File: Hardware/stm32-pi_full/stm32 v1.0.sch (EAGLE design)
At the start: 292 parts, among them J1 SOLDERJUMPERNO, J2 5-1814400-1, U1 ESP32-WROOM-32D, X1 OPAMP, Y1 6MM_3.5MM_CRYSTAL

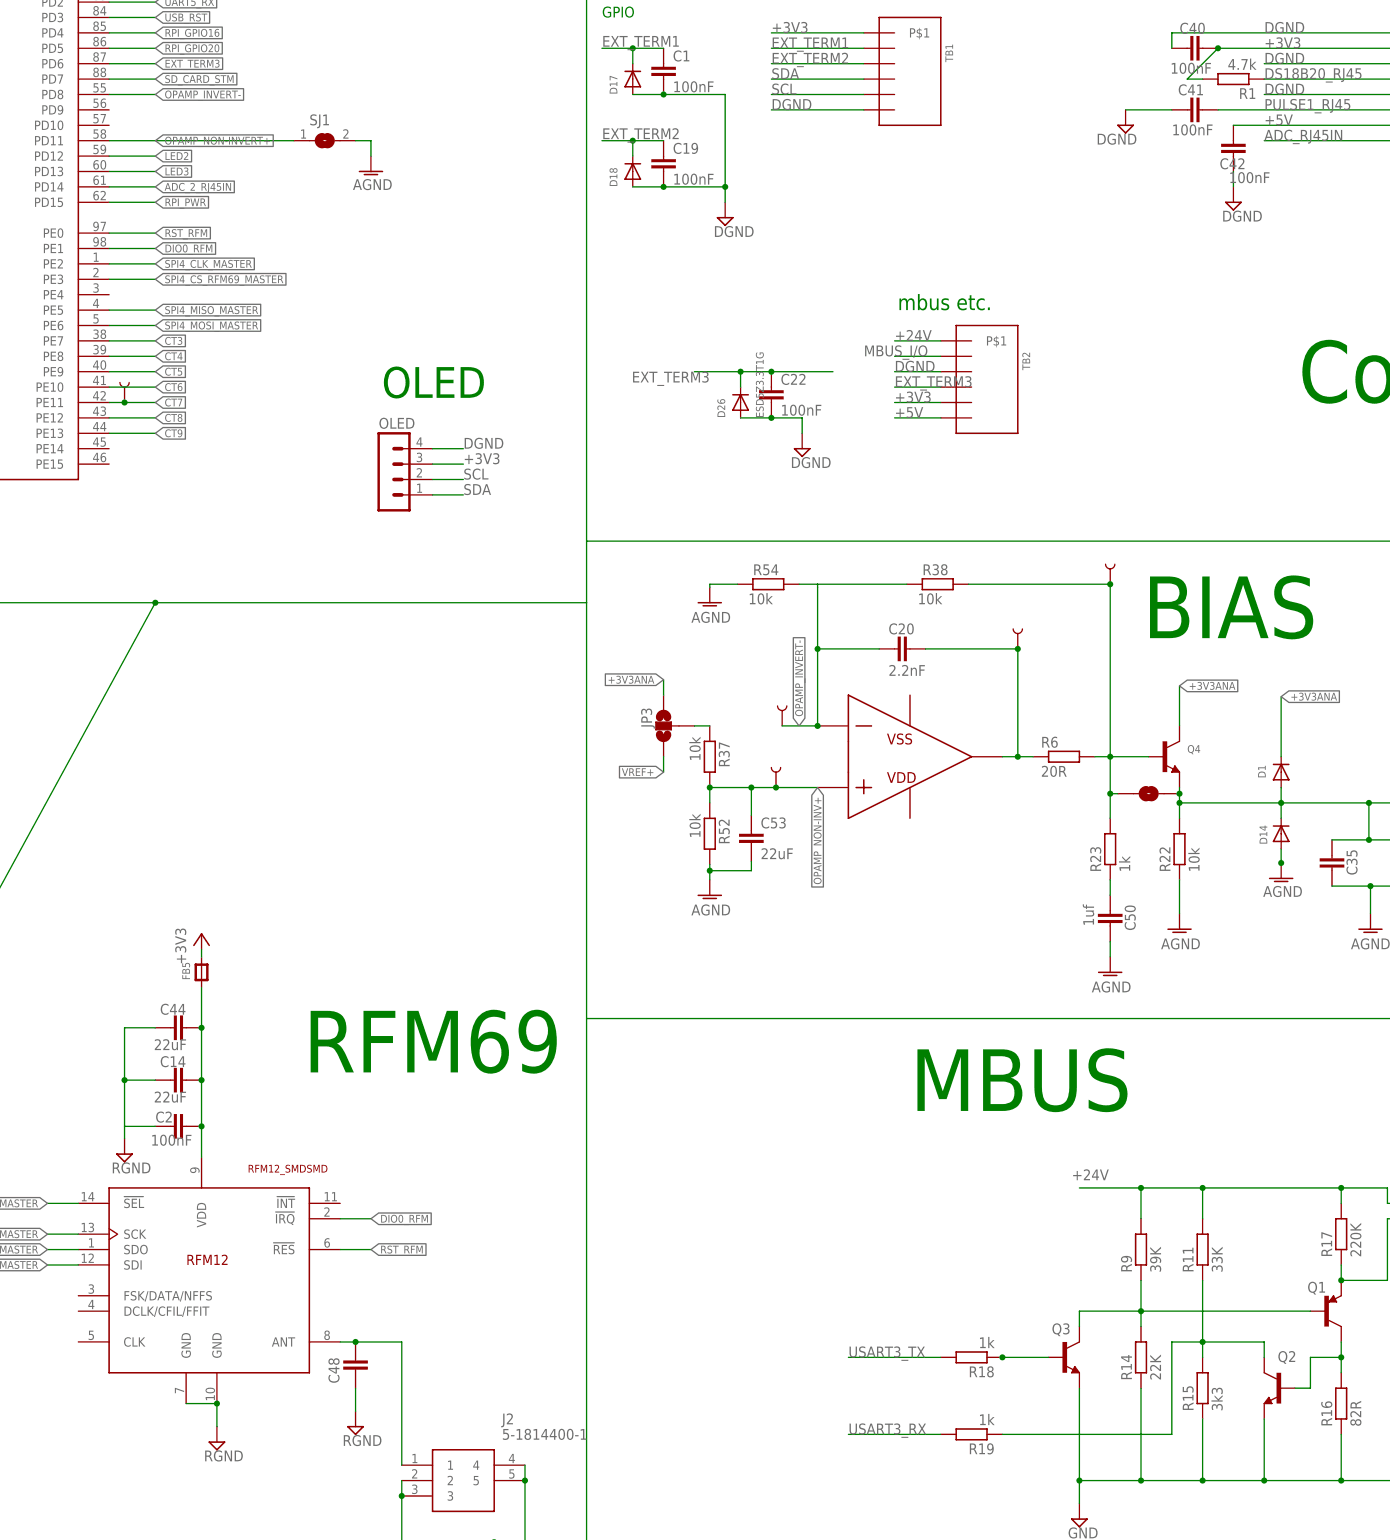
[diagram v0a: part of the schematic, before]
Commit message: UART Tx improvments and v1.0 HW change
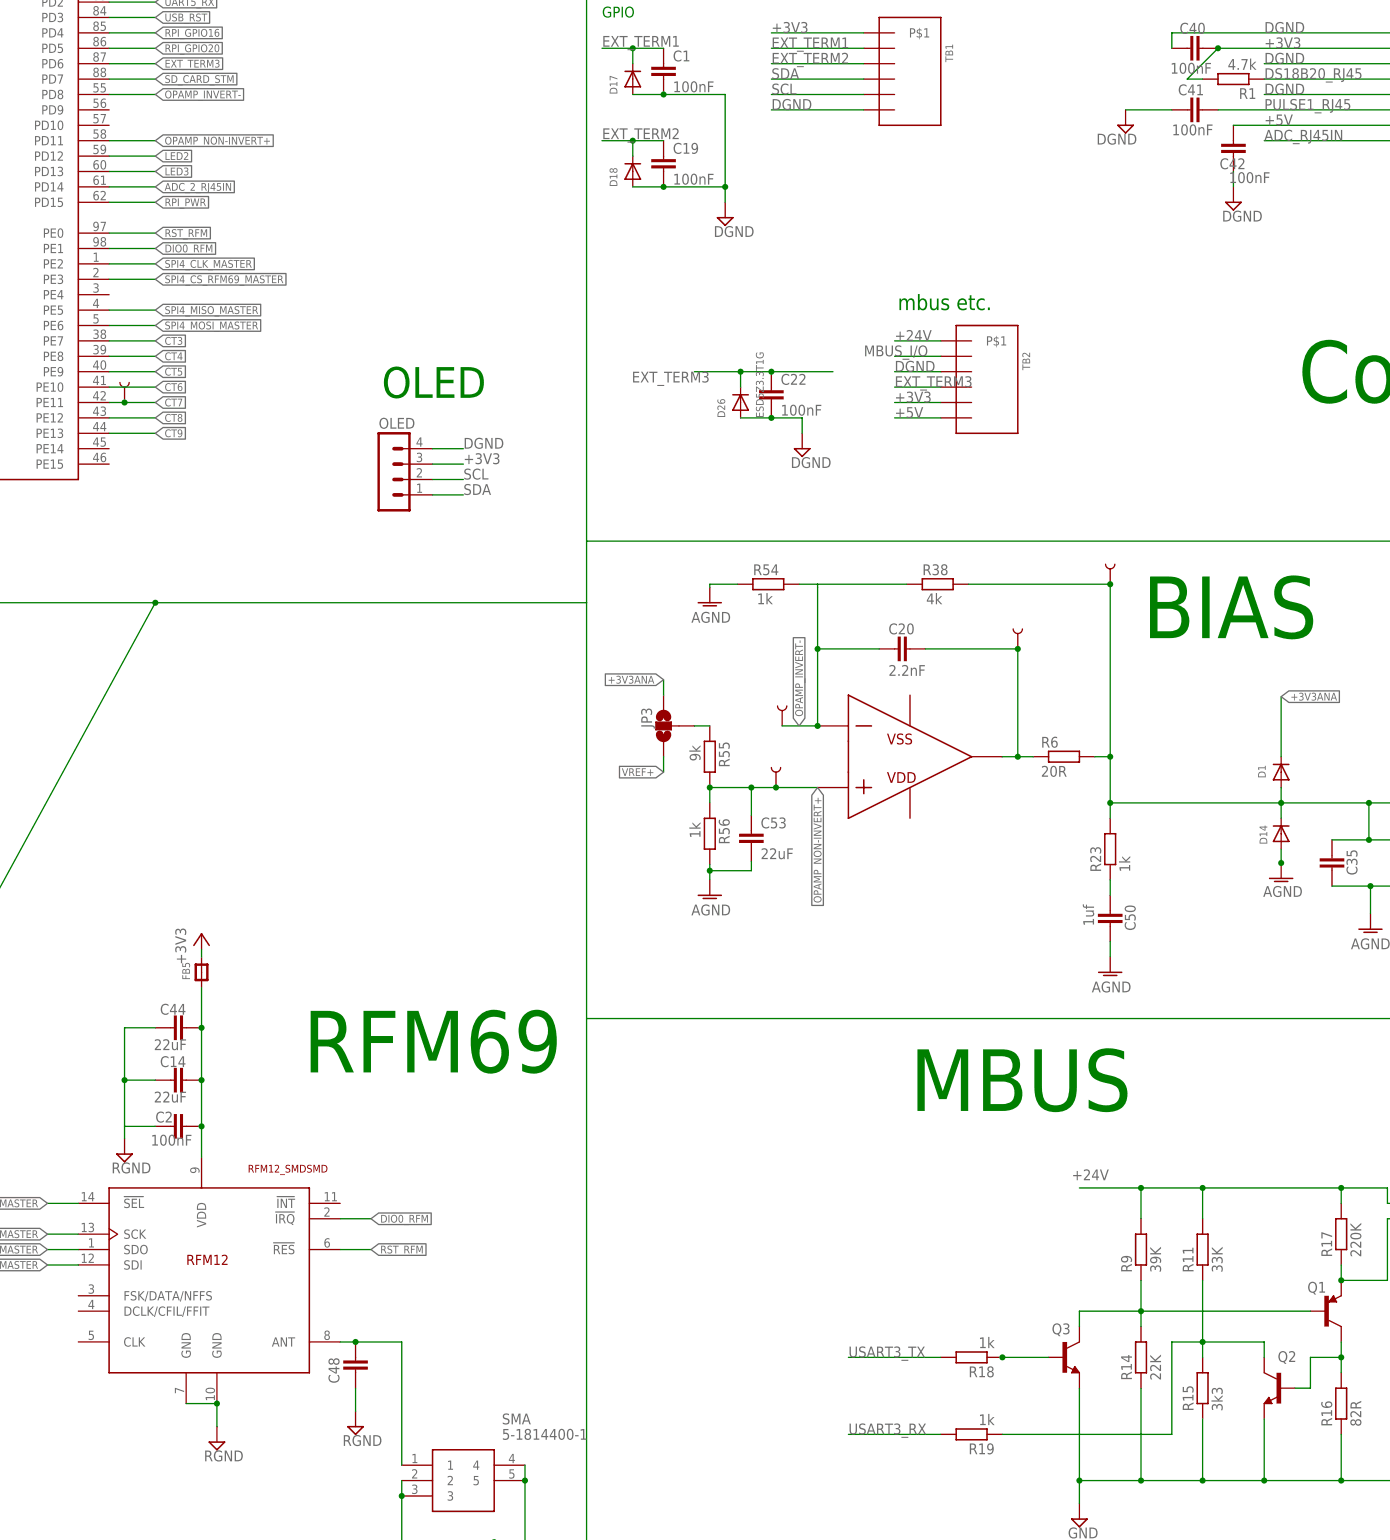
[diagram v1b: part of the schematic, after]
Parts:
- removed JP2: JUMPER-SMT_2_NO_NO-SILK, SparkFun-Jumpers:JUMPER-SMT_2_NO_NO-SILK
- removed Q4: (no value), microbuilder:TRANSISTOR_NPNWIDE
- removed R22: 10k, resistor:R-EU_R0603
- removed SJ1: (no value), jumper-con_db:SJ-CONCON
- R38: value 10k -> 4k
- R54, R56: value 10k -> 1k
- R55: value 10k -> 9k
- renumbered J2 to SMA, R37 to R55, R52 to R56
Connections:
- removed net OPAMP_FB2: JP2.1, Q4.B, R23.2, R38.1, R6.2, TP3.1
- removed net OPAMP_NON-INV+: C53.1, R55.1, R56.2, TP2.1, X1.P
- net +3V3ANA: no longer Q4.C
- net AGND: no longer R22.1, SJ1.2
- net BIAS: now also R23.2, R38.1, R6.2, TP3.1; no longer JP2.2, Q4.E, R22.2
- net OPAMP_NON-INVERT+: now also C53.1, R55.1, R56.2, TP2.1, X1.P; no longer SJ1.1

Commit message: commit v1.0 HW for prototype.
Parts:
- removed D14, D22, D23, D32, D36, D37: ESD5Z3.3T1G, microbuilder:DIODESOD-523
- removed EXPANSION: TSM-113-01-T-DV, pinhead+:PINHD-2X13SMT
- removed JP19, JP3: JUMPER-SMT_3_NO_NO-SILK, SparkFun-Jumpers:JUMPER-SMT_3_NO_NO-SILK
- removed R35, R36: 10k, rcl:R-EU_R0603
- removed SV1: (no value), con-lstb-db:MA06-1
- removed UART1: (no value), con-lstb-db:MA02-1
- removed X1: OPAMP, ngspice-simulation:OPAMP
- added D3: SCHOTTKY_MBR0520LT1GDO-219-AB(SOD123F), Diode:SCHOTTKY_MBR0520LT1GDO-219-AB(SOD123F)
- added D4: ESD5Z3.3T1G, microbuilder:DIODESOD-523
- added IC2: AD8519KS, analog-devices:AD8519KS
- added IC_VBAT: AP7313-33SRG-7, AP7313-33SRG-7:AP7313-33SRG-7
- added JP2: PINHD-2X7, Connector:PINHD-2X7
- added R22: 0R, rcl:R-EU_R0603
- added TP8: TEST-POINTPOGO_PTH, SparkFun-Connectors:TEST-POINTPOGO_PTH
- C23, C50: value 1uf -> 1uF
- C49: value 1nF -> 100nF
- C52: value 22UF -> 1uF; device rcl:C-EUC0805 -> resistor:C-EUC0603
- C7: value 22uF -> 1uF; device rcl:C-EUC0805 -> resistor:C-EUC0603
- D2: value ESD5Z3.3T1G -> SCHOTTKY_MBR0520LT1GDO-219-AB(SOD123F); device microbuilder:DIODESOD-523 -> Diode:SCHOTTKY_MBR0520LT1GDO-219-AB(SOD123F); MPN (none) -> MBR130LSFT1G
- J1, SJ14, SJ26, SJ27, SJ3, SJ32, SJ5, SJ6, SJ7: value SOLDERJUMPERNO -> JUMPER-SMT_2_NC_TRACE_NO-SILK; device SparkFun:SOLDERJUMPERNO -> SparkFun-Jumpers:JUMPER-SMT_2_NC_TRACE_NO-SILK
- Q1: value (none) -> PNP
- Q2, Q3: value (none) -> NPN
- R12, R24, R28: value 10K -> 10k
- R38: value 4k -> 39k
- R39, R40, R41: value 620 -> 620R
- R54, R56: value 1k -> 10k
- R55: value 9k -> 91k
- R6: value 20R -> 0R
- R8: value 100k -> 10k
- RB1A, RB2A, RB3A, RB4A, RB5A, RB6A, RB7A, RB8A, RB9A: value 22r -> 6R8
- RB1B, RB2B, RB3B, RB4B, RB5B, RB6B, RB7B, RB8B, RB9B: value 22r -> (none)
- USART1: value (none) -> UART1
- renumbered D40*1 to D40, UART_STM to USART1, Y1 to HSE
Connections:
- removed net 3PH_BIAS_IN: C52.1, D2.C, D32.A, LMV824.4IN+, R35.2, R36.1
- removed net CT_EX1: EXPANSION.3
- removed net CT_EX2: EXPANSION.6
- removed net CT_EX3: EXPANSION.5
- removed net CT_EX4: EXPANSION.8
- removed net CT_EX5: EXPANSION.7
- removed net CT_EX6: EXPANSION.10
- removed net IO1_EX: EXPANSION.15
- removed net IO2_EX: EXPANSION.16
- removed net IO4_EX: EXPANSION.18
- removed net IO6_EX: EXPANSION.21
- removed net IO7_EX: EXPANSION.23
- removed net N$12: JP3.2, R55.2
- removed net N$19: D37.C, R8.1
- removed net SINGLEPHASE_: D22.A, D23.C, R29.1, R43.1, R53.1
- removed net UART2_RX: STM32F303VE.PA3, SV1.4
- removed net UART2_TX: STM32F303VE.PA2, SV1.5
- removed net VDDA: C13.1, C17.1, JP19.2, STM32F303VE.VDDA
- new net N$28: JP2.13
- new net _AC1: R34.1, R43.2, VT1.TIP
- net +3V3: now also JP2.12; no longer EXPANSION.24, EXPANSION.4
- net +3V3ANA: now also C13.1, C17.1, D2.C, D4.C, IC2.+VS, R22.1, STM32F303VE.VDDA; no longer D1.C, D22.C, D32.C, JP19.1, JP3.3, R35.1
- net +5V: now also C52.1, IC_VBAT.IN, JP2.14; no longer C7.1, D36.A, EXPANSION.26, SV1.3
- net AC1: now also D1.C, D4.A, R29.1, R43.1, R53.1; no longer R34.1, R43.2, VT1.TIP
- net AGND: now also D1.A, D3.A, IC2.-VS; no longer C11.2, C37.2, C52.2, D14.A, D2.A, D23.A, EXPANSION.1, EXPANSION.2, PS1.GND, R36.2
- net BIAS: now also D2.A, D3.C, LMV824.4IN+; no longer D1.A, D14.C
- net CAN_RX: now also JP2.7; no longer EXPANSION.17
- net CAN_TX: now also JP2.5; no longer EXPANSION.19
- net DGND: now also C11.2, C37.2, C52.2, IC_VBAT.GND, JP2.2, PS1.GND; no longer EXPANSION.14, EXPANSION.25, EXPANSION.9, SV1.1
- net N$16: now also C7.1, IC_VBAT.OUT, R8.1; no longer D36.C, D37.A
- net NRST_STM: no longer SV1.6
- net OPAMP_INVERT-: now also IC2.IN-; no longer X1.N
- net OPAMP_NON-INVERT+: now also IC2.IN+; no longer X1.P
- net OPAMP_OUT: now also IC2.OUT; no longer X1.VOUT
- net SCL: now also JP2.10; no longer EXPANSION.22
- net SDA: now also JP2.8; no longer EXPANSION.20
- net UART1_RX: no longer UART1.1
- net UART1_TX: no longer UART1.2
- net VREF+: now also R22.2, R55.2, TP8.1; no longer JP19.3, JP3.1
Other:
- moved on the sheet: C52, C7, CV1, CV2, CV3, CV4, D1, G1, LMV824, R25, R26, R27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

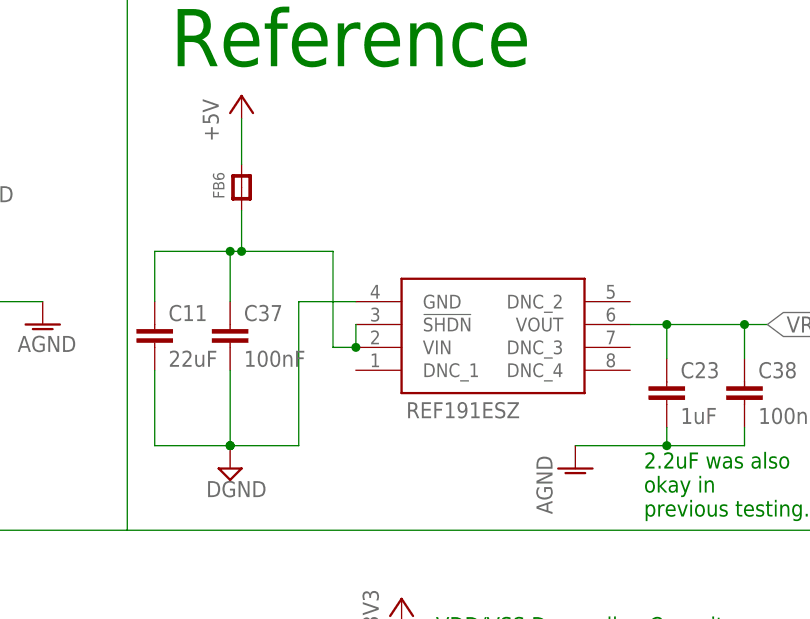
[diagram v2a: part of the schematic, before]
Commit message: correct rotation of p&p'd parts.
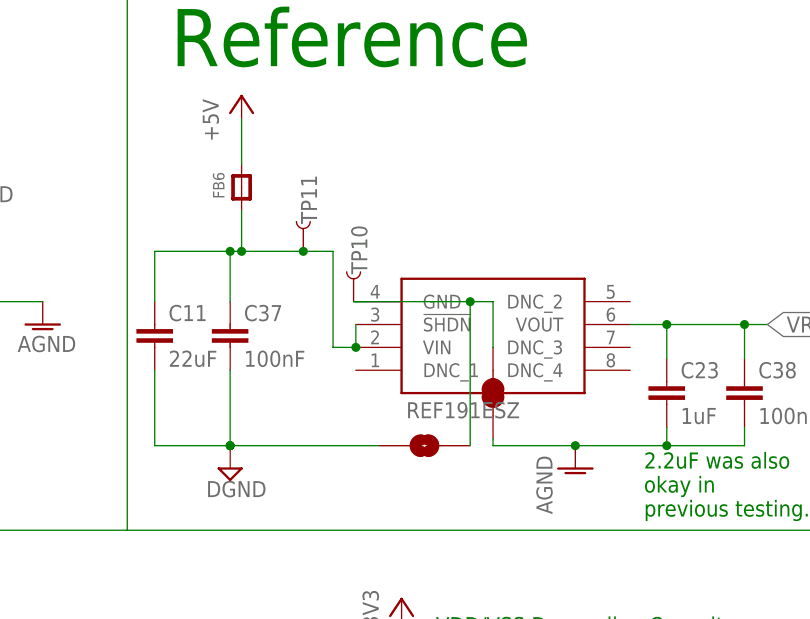
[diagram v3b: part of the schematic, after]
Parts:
- added SJ1: JUMPER-SMT_2_NC_TRACE_NO-SILK, SparkFun-Jumpers:JUMPER-SMT_2_NC_TRACE_NO-SILK
- added SJ2: JUMPER-SMT_2_NO_SILK, SparkFun-Jumpers:JUMPER-SMT_2_NO_SILK
- added TP10, TP11: TEST-POINTPOGO_PTH, SparkFun-Connectors:TEST-POINTPOGO_PTH
- renumbered PS1 to REF19X
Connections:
- new net N$12: REF19X.GND, SJ1.2, SJ2.2, TP10.1
- net +5V_REF: now also TP11.1
- net AGND: now also SJ1.1
- net DGND: now also SJ2.1; no longer REF19X.GND
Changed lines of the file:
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@@
 <part name="C33" library="rcl" library_urn="urn:adsk.eagle:library:334" deviceset="C-EU" device="C0805" package3d_urn="urn:adsk.eagle:package:23617/2" value="22uF"/>
 <part name="SJ14" library="SparkFun-Jumpers" library_urn="urn:adsk.eagle:library:528" deviceset="JUMPER-SMT_2_NC_TRACE" device="_NO-SILK" package3d_urn="urn:adsk.eagle:package:39286/1"/>
-<part name="PS1" library="LT1461AIS8" deviceset="LT1461AIS8-3.3#PBF" device="" value="REF191ESZ">
+<part name="REF19X" library="LT1461AIS8" deviceset="LT1461AIS8-3.3#PBF" device="" value="REF191ESZ">
 <attribute name="MPN" value="REF191ESZ"/>
 </part>
@@
 <part name="D1" library="microbuilder" deviceset="DIODE" device="SOD-523" value="ESD5Z3.3T1G"/>
 <part name="D4" library="microbuilder" deviceset="DIODE" device="SOD-523" value="ESD5Z3.3T1G"/>
+<part name="TP10" library="SparkFun-Connectors" deviceset="TEST-POINT" device="POGO_PTH" value="TEST-POINTPOGO_PTH"/>
+<part name="TP11" library="SparkFun-Connectors" deviceset="TEST-POINT" device="POGO_PTH" value="TEST-POINTPOGO_PTH"/>
+<part name="SJ1" library="SparkFun-Jumpers" library_urn="urn:adsk.eagle:library:528" deviceset="JUMPER-SMT_2_NC_TRACE" device="_NO-SILK" package3d_urn="urn:adsk.eagle:package:39286/1"/>
+<part name="SJ2" library="SparkFun-Jumpers" library_urn="urn:adsk.eagle:library:528" deviceset="JUMPER-SMT_2_NO" device="_SILK" package3d_urn="urn:adsk.eagle:package:39279/1" value="JUMPER-SMT_2_NO_SILK"/>
 </parts>
 <sheets>
@@
 </instance>
 <instance part="SJ14" gate="G$1" x="-119.38" y="2.54" smashed="yes"/>
-<instance part="PS1" gate="G$1" x="134.62" y="162.56" smashed="yes" rot="MR180">
+<instance part="REF19X" gate="G$1" x="134.62" y="162.56" smashed="yes" rot="MR180">
 <attribute name="MPN" x="140.208" y="159.004" size="1.778" layer="96" rot="MR180"/>
 </instance>
@@
 <attribute name="NAME" x="376.174" y="246.38" size="1.27" layer="95" rot="R90"/>
 </instance>
+<instance part="TP10" gate="G$1" x="134.366" y="170.18" smashed="yes" rot="R90">
+<attribute name="NAME" x="135.89" y="173.228" size="1.778" layer="95" font="vector" rot="R90"/>
+</instance>
+<instance part="TP11" gate="G$1" x="128.778" y="175.768" smashed="yes" rot="R90">
+<attribute name="NAME" x="130.302" y="178.816" size="1.778" layer="95" font="vector" rot="R90"/>
+</instance>
+<instance part="SJ1" gate="G$1" x="149.86" y="160.02" smashed="yes" rot="R90"/>
+<instance part="SJ2" gate="G$1" x="142.24" y="154.178" smashed="yes"/>
 </instances>
 <busses>
@@
 <wire x1="112.268" y1="162.56" x2="112.268" y2="154.178" width="0.1524" layer="91"/>
 <wire x1="112.268" y1="154.178" x2="120.65" y2="154.178" width="0.1524" layer="91"/>
-<pinref part="PS1" gate="G$1" pin="GND"/>
-<wire x1="134.62" y1="170.18" x2="128.27" y2="170.18" width="0.1524" layer="91"/>
-<wire x1="128.27" y1="170.18" x2="128.27" y2="154.178" width="0.1524" layer="91"/>
-<wire x1="128.27" y1="154.178" x2="120.65" y2="154.178" width="0.1524" layer="91"/>
 <junction x="120.65" y="154.178"/>
 <pinref part="C37" gate="G$1" pin="2"/>
@@
 <junction x="120.65" y="154.178"/>
 <pinref part="SUPPLY22" gate="G$1" pin="DGND"/>
+<pinref part="SJ2" gate="G$1" pin="1"/>
+<wire x1="137.16" y1="154.178" x2="120.65" y2="154.178" width="0.1524" layer="91"/>
 </segment>
 </net>
@@
 </segment>
 <segment>
-<pinref part="PS1" gate="G$1" pin="VOUT"/>
+<pinref part="REF19X" gate="G$1" pin="VOUT"/>
 <wire x1="165.1" y1="167.64" x2="169.164" y2="167.64" width="0.1524" layer="91"/>
 <label x="180.34" y="167.64" size="1.778" layer="95" xref="yes"/>
@@
 <wire x1="169.164" y1="154.178" x2="159.004" y2="154.178" width="0.1524" layer="91"/>
 <pinref part="AGND12" gate="VR1" pin="AGND"/>
+<pinref part="SJ1" gate="G$1" pin="1"/>
+<wire x1="149.86" y1="154.94" x2="149.86" y2="154.178" width="0.1524" layer="91"/>
+<wire x1="149.86" y1="154.178" x2="159.004" y2="154.178" width="0.1524" layer="91"/>
+<junction x="159.004" y="154.178"/>
 </segment>
 <segment>
@@
 <wire x1="112.268" y1="175.768" x2="120.65" y2="175.768" width="0.1524" layer="91"/>
 <wire x1="120.65" y1="175.768" x2="121.92" y2="175.768" width="0.1524" layer="91"/>
-<pinref part="PS1" gate="G$1" pin="VIN"/>
-<wire x1="121.92" y1="175.768" x2="132.08" y2="175.768" width="0.1524" layer="91"/>
+<pinref part="REF19X" gate="G$1" pin="VIN"/>
+<wire x1="121.92" y1="175.768" x2="128.778" y2="175.768" width="0.1524" layer="91"/>
+<wire x1="128.778" y1="175.768" x2="132.08" y2="175.768" width="0.1524" layer="91"/>
 <wire x1="134.62" y1="165.1" x2="132.08" y2="165.1" width="0.1524" layer="91"/>
 <wire x1="132.08" y1="165.1" x2="132.08" y2="175.768" width="0.1524" layer="91"/>
-<pinref part="PS1" gate="G$1" pin="!SHDN"/>
+<pinref part="REF19X" gate="G$1" pin="!SHDN"/>
 <wire x1="134.62" y1="167.64" x2="134.62" y2="165.1" width="0.1524" layer="91"/>
 <junction x="134.62" y="165.1"/>
@@
 <wire x1="121.92" y1="180.34" x2="121.92" y2="175.768" width="0.1524" layer="91"/>
 <junction x="121.92" y="175.768"/>
+<pinref part="TP11" gate="G$1" pin="1"/>
+<junction x="128.778" y="175.768"/>
 </segment>
 </net>
@@
 </segment>
 </net>
+<net name="N$12" class="2">
+<segment>
+<wire x1="149.86" y1="170.18" x2="149.86" y2="165.1" width="0.1524" layer="91"/>
+<pinref part="REF19X" gate="G$1" pin="GND"/>
+<wire x1="134.62" y1="170.18" x2="147.32" y2="170.18" width="0.1524" layer="91"/>
+<wire x1="147.32" y1="170.18" x2="149.86" y2="170.18" width="0.1524" layer="91"/>
+<wire x1="134.62" y1="170.18" x2="134.366" y2="170.18" width="0.1524" layer="91"/>
+<pinref part="TP10" gate="G$1" pin="1"/>
+<wire x1="134.366" y1="170.18" x2="135.89" y2="170.18" width="0.1524" layer="91"/>
+<pinref part="SJ1" gate="G$1" pin="2"/>
+<pinref part="SJ2" gate="G$1" pin="2"/>
+<wire x1="147.32" y1="154.178" x2="147.32" y2="170.18" width="0.1524" layer="91"/>
+<junction x="147.32" y="170.18"/>
+</segment>
+</net>
